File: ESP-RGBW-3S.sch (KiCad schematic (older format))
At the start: 41 parts, among them J1 12V IN, J2 PROG, J3 LED Str., J4 Temp. S., J5 Light. S., J6 PIR, Q1 IRLML0040TRPBF, Q2 IRLML0040TRPBF, Q3 IRLML0040TRPBF, Q4 IRLML0040TRPBF, SW1 Flash, U2 ESP-12E, U4 DCDC_LM2596

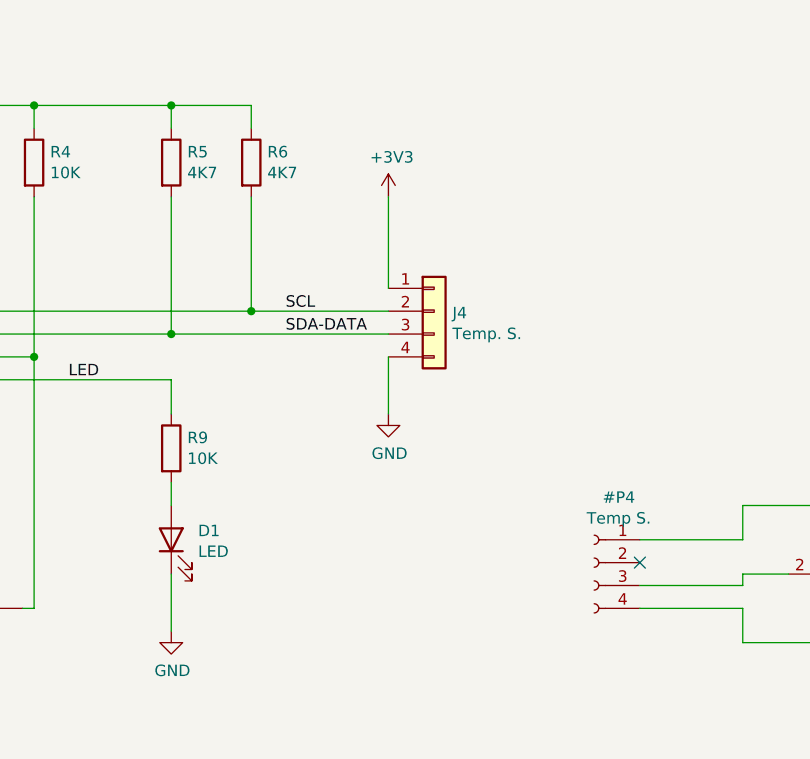
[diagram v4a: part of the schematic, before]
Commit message: oprional pull-down resistors for GPIO 4-5
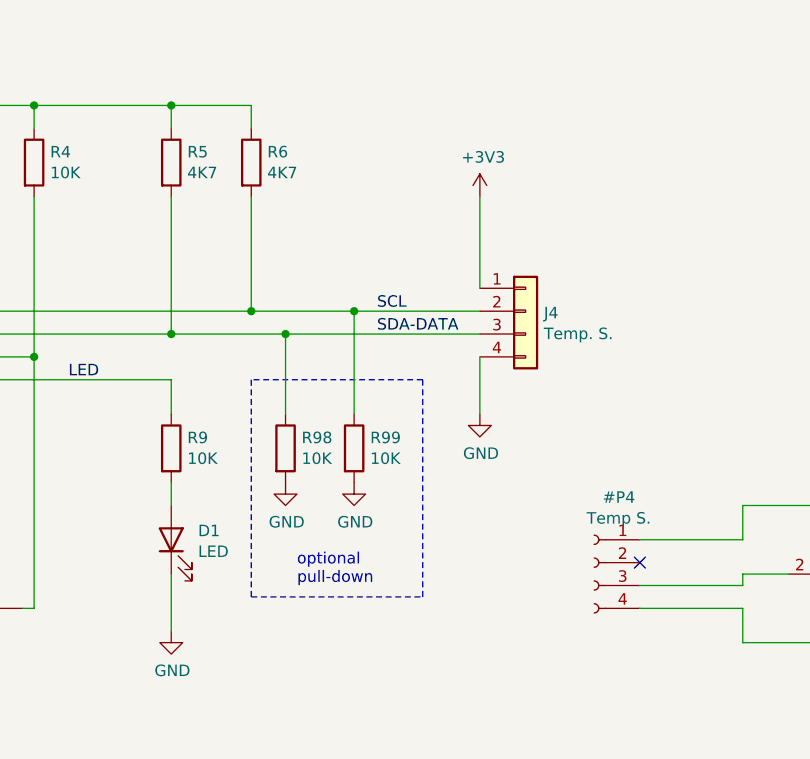
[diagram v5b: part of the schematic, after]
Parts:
- added R98, R99: 10K, Resistor_SMD:R_0805_2012Metric, symbol Device:R
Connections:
- net GND: now also R98.2, R99.2
- net SCL: now also R99.1
- net SDA-DATA: now also R98.1
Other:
- moved on the sheet: J4
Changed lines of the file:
@@
 L power:GND #PWR03
 U 1 1 609124D8
-P 6550 2200
-F 0 "#PWR03" H 6550 1950 50  0001 C CNN
-F 1 "GND" H 6555 2027 50  0000 C CNN
-F 2 "" H 6550 2200 50  0001 C CNN
-F 3 "" H 6550 2200 50  0001 C CNN
-	1    6550 2200
-	1    0    0    -1
-$EndComp
-Wire Wire Line
-	6550 1950 6550 2200
+P 6950 2200
+F 0 "#PWR03" H 6950 1950 50  0001 C CNN
+F 1 "GND" H 6955 2027 50  0000 C CNN
+F 2 "" H 6950 2200 50  0001 C CNN
+F 3 "" H 6950 2200 50  0001 C CNN
+	1    6950 2200
+	1    0    0    -1
+$EndComp
+Wire Wire Line
+	6950 1950 6950 2200
 Wire Wire Line
 	4100 1750 5950 1750
 Wire Wire Line
-	6550 1250 6550 1650
+	6950 1250 6950 1650
 $Comp
 L Device:R R6
@@
 Wire Wire Line
 	5950 1250 5950 1750
-Connection ~ 5950 1750
-Wire Wire Line
-	5950 1750 6550 1750
+Wire Wire Line
+	5950 1750 6400 1750
 Wire Wire Line
 	5600 1250 5600 1850
 Wire Wire Line
 	4100 1850 5600 1850
-Connection ~ 5600 1850
-Wire Wire Line
-	5600 1850 6550 1850
+Wire Wire Line
+	5600 1850 6100 1850
 $Comp
 L Connector_Generic:Conn_01x04 J4
 U 1 1 6090F6BA
-P 6750 1750
-F 0 "J4" H 6830 1742 50  0000 L CNN
-F 1 "Temp. S." H 6830 1651 50  0000 L CNN
-F 2 "Connector_Molex:Molex_KK-254_AE-6410-04A_1x04_P2.54mm_Vertical" H 6750 1750 50  0001 C CNN
-F 3 "~" H 6750 1750 50  0001 C CNN
-	1    6750 1750
-	1    0    0    -1
-$EndComp
-Text Label 6100 1850 0    50   ~ 0
+P 7150 1750
+F 0 "J4" H 7230 1742 50  0000 L CNN
+F 1 "Temp. S." H 7230 1651 50  0000 L CNN
+F 2 "Connector_Molex:Molex_KK-254_AE-6410-04A_1x04_P2.54mm_Vertical" H 7150 1750 50  0001 C CNN
+F 3 "~" H 7150 1750 50  0001 C CNN
+	1    7150 1750
+	1    0    0    -1
+$EndComp
+Text Label 6500 1850 0    50   ~ 0
 SDA-DATA
-Text Label 6100 1750 0    50   ~ 0
+Text Label 6500 1750 0    50   ~ 0
 SCL
 Wire Wire Line
@@
 L power:+3V3 #PWR02
 U 1 1 609155BA
-P 6550 1250
-F 0 "#PWR02" H 6550 1100 50  0001 C CNN
-F 1 "+3V3" H 6565 1423 50  0000 C CNN
-F 2 "" H 6550 1250 50  0001 C CNN
-F 3 "" H 6550 1250 50  0001 C CNN
-	1    6550 1250
+P 6950 1250
+F 0 "#PWR02" H 6950 1100 50  0001 C CNN
+F 1 "+3V3" H 6965 1423 50  0000 C CNN
+F 2 "" H 6950 1250 50  0001 C CNN
+F 3 "" H 6950 1250 50  0001 C CNN
+	1    6950 1250
 	1    0    0    -1
 $EndComp
@@
 	9550 600  9150 600
 $Comp
-L power:+3V3 #PWR?
+L power:+3V3 #PWR0108
 U 1 1 60B5BA99
 P 9150 600
-F 0 "#PWR?" H 9150 450 50  0001 C CNN
+F 0 "#PWR0108" H 9150 450 50  0001 C CNN
 F 1 "+3V3" H 9165 773 50  0000 C CNN
 F 2 "" H 9150 600 50  0001 C CNN
@@
 	9900 1750 9900 1500
 $Comp
-L power:GND #PWR?
+L power:GND #PWR0109
 U 1 1 60B6FB81
 P 9900 2150
-F 0 "#PWR?" H 9900 1900 50  0001 C CNN
+F 0 "#PWR0109" H 9900 1900 50  0001 C CNN
 F 1 "GND" H 9905 1977 50  0000 C CNN
 F 2 "" H 9900 2150 50  0001 C CNN
@@
 Text Notes 9000 1950 0    50   ~ 0
 optional\npull-down
+Connection ~ 5600 1850
+Connection ~ 5950 1750
+$Comp
+L Device:R R98
+U 1 1 60ADF053
+P 6100 2350
+F 0 "R98" H 6170 2396 50  0000 L CNN
+F 1 "10K" H 6170 2305 50  0000 L CNN
+F 2 "Resistor_SMD:R_0805_2012Metric" V 6030 2350 50  0001 C CNN
+F 3 "~" H 6100 2350 50  0001 C CNN
+	1    6100 2350
+	1    0    0    -1
+$EndComp
+$Comp
+L Device:R R99
+U 1 1 60ADFAE9
+P 6400 2350
+F 0 "R99" H 6470 2396 50  0000 L CNN
+F 1 "10K" H 6470 2305 50  0000 L CNN
+F 2 "Resistor_SMD:R_0805_2012Metric" V 6330 2350 50  0001 C CNN
+F 3 "~" H 6400 2350 50  0001 C CNN
+	1    6400 2350
+	1    0    0    -1
+$EndComp
+Wire Wire Line
+	6100 1850 6100 2200
+Connection ~ 6100 1850
+Wire Wire Line
+	6100 1850 6950 1850
+Wire Wire Line
+	6400 1750 6400 2200
+Connection ~ 6400 1750
+Wire Wire Line
+	6400 1750 6950 1750
+$Comp
+L power:GND #PWR0110
+U 1 1 60AEF13E
+P 6100 2500
+F 0 "#PWR0110" H 6100 2250 50  0001 C CNN
+F 1 "GND" H 6105 2327 50  0000 C CNN
+F 2 "" H 6100 2500 50  0001 C CNN
+F 3 "" H 6100 2500 50  0001 C CNN
+	1    6100 2500
+	1    0    0    -1
+$EndComp
+$Comp
+L power:GND #PWR0111
+U 1 1 60AEF684
+P 6400 2500
+F 0 "#PWR0111" H 6400 2250 50  0001 C CNN
+F 1 "GND" H 6405 2327 50  0000 C CNN
+F 2 "" H 6400 2500 50  0001 C CNN
+F 3 "" H 6400 2500 50  0001 C CNN
+	1    6400 2500
+	1    0    0    -1
+$EndComp
+Wire Notes Line
+	5950 2050 5950 3000
+Wire Notes Line
+	5950 3000 6700 3000
+Wire Notes Line
+	6700 3000 6700 2050
+Wire Notes Line
+	6700 2050 5950 2050
+Text Notes 6150 2950 0    50   ~ 0
+optional\npull-down
 $EndSCHEMATC

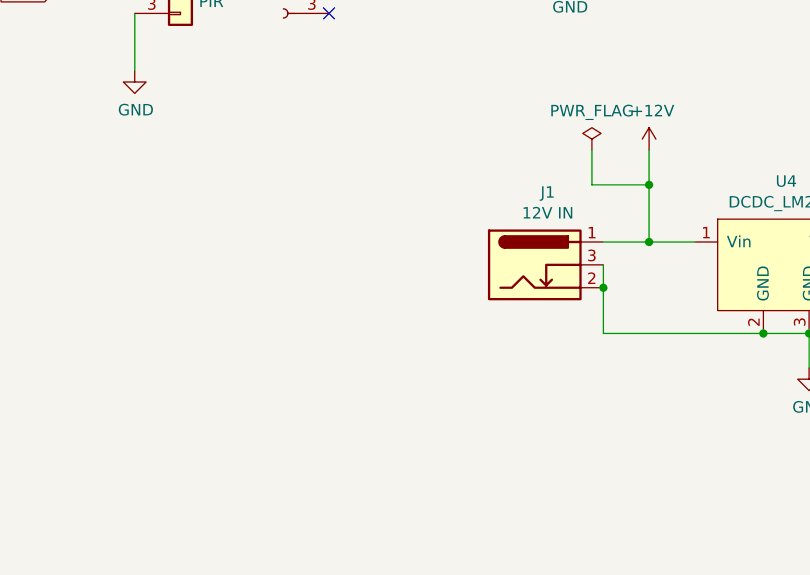
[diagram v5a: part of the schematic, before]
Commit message: oprional input power terminal
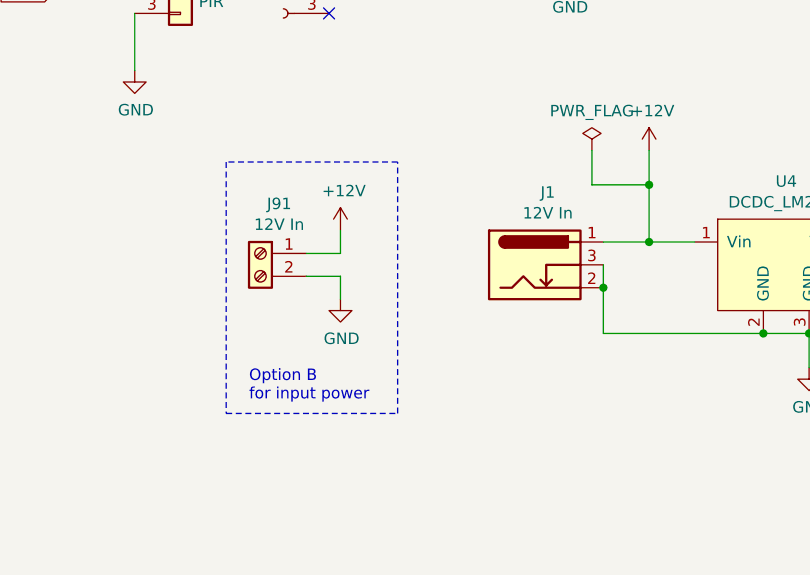
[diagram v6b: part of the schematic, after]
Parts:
- added J91: 12V In, symbol Connector:Screw_Terminal_01x02
- J1: value 12V IN -> 12V In
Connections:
- net +12V: now also J91.1 (Pin_1)
- net GND: now also J91.2 (Pin_2)
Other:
- note added: "Option B\nfor input power"
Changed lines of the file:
@@
 P 8550 5800
 F 0 "J1" H 8607 6117 50  0000 C CNN
-F 1 "12V IN" H 8607 6026 50  0000 C CNN
+F 1 "12V In" H 8607 6026 50  0000 C CNN
 F 2 "Connector_BarrelJack:BarrelJack_Horizontal" H 8600 5760 50  0001 C CNN
 F 3 "~" H 8600 5760 50  0001 C CNN
@@
 L power:+12V #PWR014
 U 1 1 60962EEC
-P 9050 5300
-F 0 "#PWR014" H 9050 5150 50  0001 C CNN
-F 1 "+12V" H 9065 5473 50  0000 C CNN
-F 2 "" H 9050 5300 50  0001 C CNN
-F 3 "" H 9050 5300 50  0001 C CNN
-	1    9050 5300
+P 7700 5650
+F 0 "#PWR014" H 7700 5500 50  0001 C CNN
+F 1 "+12V" H 7715 5823 50  0000 C CNN
+F 2 "" H 7700 5650 50  0001 C CNN
+F 3 "" H 7700 5650 50  0001 C CNN
+	1    7700 5650
 	1    0    0    -1
 $EndComp
@@
 Text Notes 6150 2950 0    50   ~ 0
 optional\npull-down
+$Comp
+L Connector:Screw_Terminal_01x02 J91
+U 1 1 60B29600
+P 7350 5750
+F 0 "J91" H 7268 5967 50  0000 C CNN
+F 1 "12V In" H 7268 5876 50  0000 C CNN
+F 2 "" H 7350 5750 50  0001 C CNN
+F 3 "~" H 7350 5750 50  0001 C CNN
+	1    7350 5750
+	-1   0    0    -1
+$EndComp
+$Comp
+L power:GND #PWR0112
+U 1 1 60B3AF54
+P 7700 5950
+F 0 "#PWR0112" H 7700 5700 50  0001 C CNN
+F 1 "GND" H 7705 5777 50  0000 C CNN
+F 2 "" H 7700 5950 50  0001 C CNN
+F 3 "" H 7700 5950 50  0001 C CNN
+	1    7700 5950
+	1    0    0    -1
+$EndComp
+$Comp
+L power:+12V #PWR0113
+U 1 1 60B3BF7D
+P 9050 5300
+F 0 "#PWR0113" H 9050 5150 50  0001 C CNN
+F 1 "+12V" H 9065 5473 50  0000 C CNN
+F 2 "" H 9050 5300 50  0001 C CNN
+F 3 "" H 9050 5300 50  0001 C CNN
+	1    9050 5300
+	1    0    0    -1
+$EndComp
+Wire Wire Line
+	7550 5750 7700 5750
+Wire Wire Line
+	7700 5750 7700 5650
+Wire Wire Line
+	7550 5850 7700 5850
+Wire Wire Line
+	7700 5850 7700 5950
+Wire Notes Line
+	7200 5350 7200 6450
+Wire Notes Line
+	7200 6450 7950 6450
+Wire Notes Line
+	7950 6450 7950 5350
+Wire Notes Line
+	7950 5350 7200 5350
+Text Notes 7300 6400 0    50   ~ 0
+Option B\nfor input power
 $EndSCHEMATC

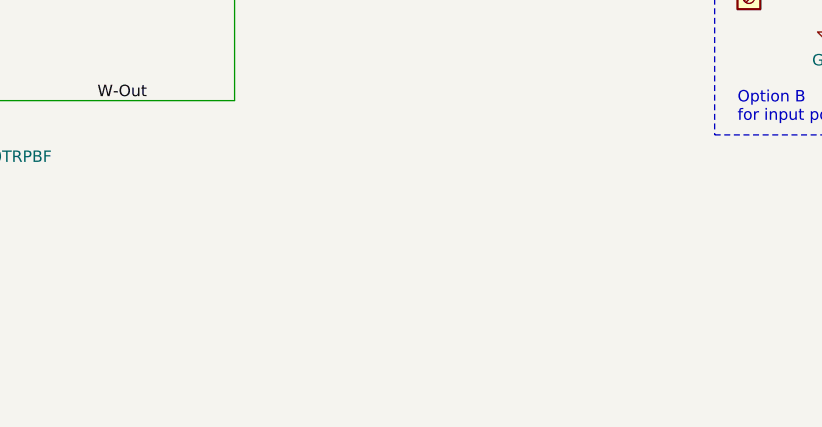
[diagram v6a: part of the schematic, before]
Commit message: alternative DC-DC convertor (MP1584)
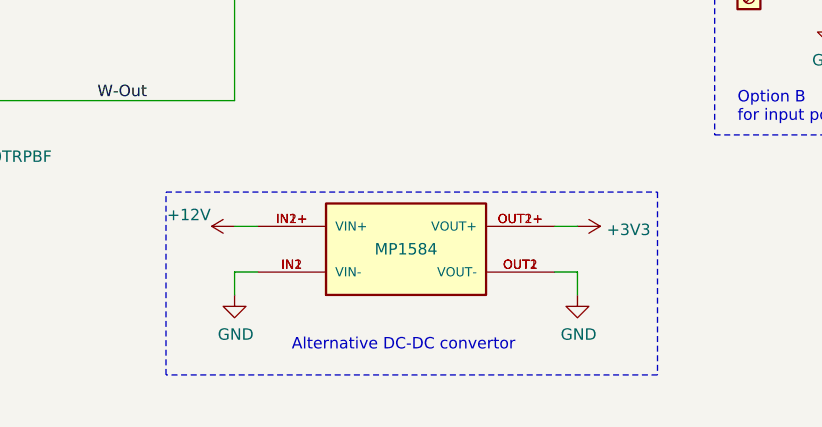
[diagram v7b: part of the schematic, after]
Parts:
- added U94: MP1584, MP1584:DC-BRICK, symbol MP1584:MP1584
- J91: footprint (none) -> TerminalBlock_Phoenix:TerminalBlock_Phoenix_MKDS-1,5-2_1x02_P5.00mm_Horizontal
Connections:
- net +12V: now also U94.IN1+ (VIN+), U94.IN2+ (VIN+)
- net +3V3: now also U94.OUT1+ (VOUT+), U94.OUT2+ (VOUT+)
- net GND: now also U94.IN1 (VIN-), U94.IN2 (VIN-), U94.OUT1 (VOUT-), U94.OUT2 (VOUT-)
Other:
- note added: "Alternative DC-DC convertor"
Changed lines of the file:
@@
 F 0 "J91" H 7268 5967 50  0000 C CNN
 F 1 "12V In" H 7268 5876 50  0000 C CNN
-F 2 "" H 7350 5750 50  0001 C CNN
+F 2 "TerminalBlock_Phoenix:TerminalBlock_Phoenix_MKDS-1,5-2_1x02_P5.00mm_Horizontal" H 7350 5750 50  0001 C CNN
 F 3 "~" H 7350 5750 50  0001 C CNN
 	1    7350 5750
@@
 Text Notes 7300 6400 0    50   ~ 0
 Option B\nfor input power
+$Comp
+L MP1584:MP1584 U94
+U 1 1 60B2F407
+P 5800 6950
+F 0 "U94" H 5800 6950 50  0001 L BNN
+F 1 "MP1584" H 5850 6950 50  0000 C CNN
+F 2 "MP1584:DC-BRICK" H 5800 6950 50  0001 L BNN
+F 3 "" H 5800 6950 50  0001 L BNN
+	1    5800 6950
+	1    0    0    -1
+$EndComp
+$Comp
+L power:GND #PWR0114
+U 1 1 60B307DC
+P 6600 7150
+F 0 "#PWR0114" H 6600 6900 50  0001 C CNN
+F 1 "GND" H 6605 6977 50  0000 C CNN
+F 2 "" H 6600 7150 50  0001 C CNN
+F 3 "" H 6600 7150 50  0001 C CNN
+	1    6600 7150
+	1    0    0    -1
+$EndComp
+$Comp
+L power:+3V3 #PWR0115
+U 1 1 60B4A7A1
+P 6600 6850
+F 0 "#PWR0115" H 6600 6700 50  0001 C CNN
+F 1 "+3V3" V 6615 6978 50  0000 L CNN
+F 2 "" H 6600 6850 50  0001 C CNN
+F 3 "" H 6600 6850 50  0001 C CNN
+	1    6600 6850
+	0    1    1    0
+$EndComp
+$Comp
+L power:+12V #PWR0116
+U 1 1 60B535FA
+P 5100 6850
+F 0 "#PWR0116" H 5100 6700 50  0001 C CNN
+F 1 "+12V" V 5150 7050 50  0000 C CNN
+F 2 "" H 5100 6850 50  0001 C CNN
+F 3 "" H 5100 6850 50  0001 C CNN
+	1    5100 6850
+	0    -1   -1   0
+$EndComp
+$Comp
+L power:GND #PWR0117
+U 1 1 60B53EF4
+P 5100 7150
+F 0 "#PWR0117" H 5100 6900 50  0001 C CNN
+F 1 "GND" H 5105 6977 50  0000 C CNN
+F 2 "" H 5100 7150 50  0001 C CNN
+F 3 "" H 5100 7150 50  0001 C CNN
+	1    5100 7150
+	1    0    0    -1
+$EndComp
+Wire Wire Line
+	5200 7050 5100 7050
+Wire Wire Line
+	5100 7050 5100 7150
+Wire Wire Line
+	6500 7050 6600 7050
+Wire Wire Line
+	6600 7050 6600 7150
+Wire Wire Line
+	6600 6850 6500 6850
+Wire Wire Line
+	5100 6850 5200 6850
+Wire Notes Line
+	4800 6700 6950 6700
+Wire Notes Line
+	6950 6700 6950 7500
+Wire Notes Line
+	6950 7500 4800 7500
+Wire Notes Line
+	4800 7500 4800 6700
+Text Notes 5350 7400 0    50   ~ 0
+Alternative DC-DC convertor
 $EndSCHEMATC

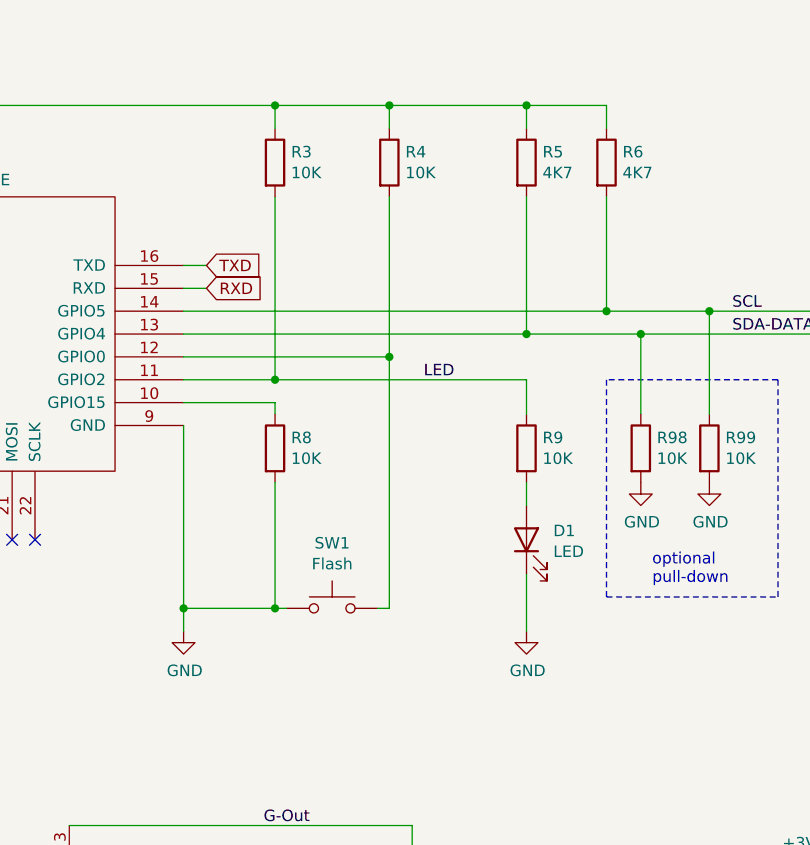
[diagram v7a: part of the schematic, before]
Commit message: status LED controlled by low-velef on mcu pin
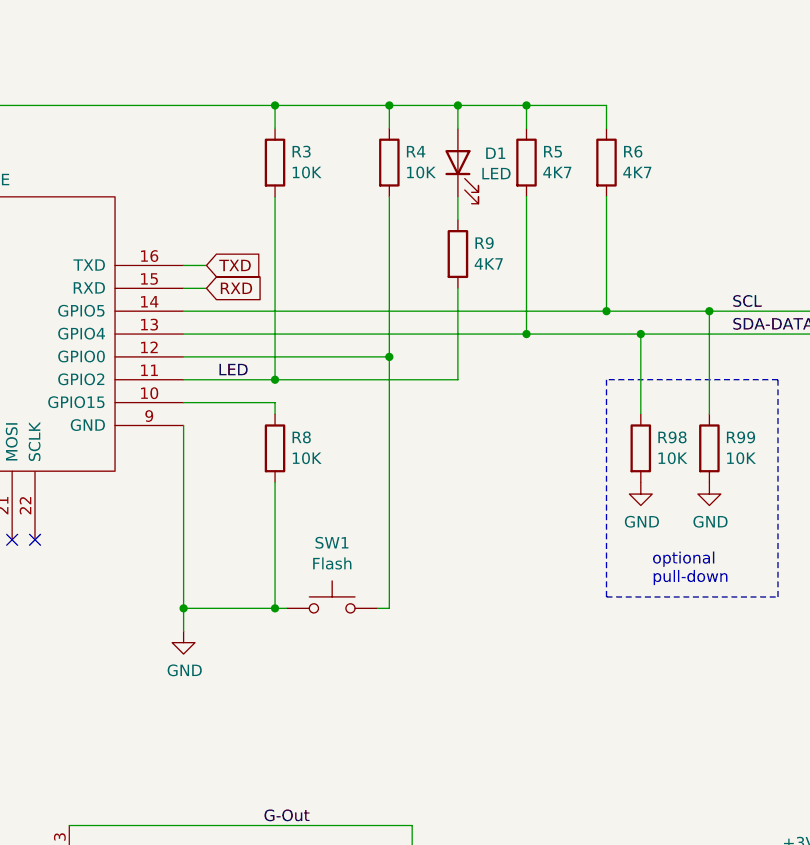
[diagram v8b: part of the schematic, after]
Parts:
- R9: value 10K -> 4K7
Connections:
- net +3V3: now also D1.2 (A)
- net GND: no longer D1.1 (K)
- net LED: now also R9.2; no longer R9.1
- new net: D1.1 (K), R9.1
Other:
- moved on the sheet: D1, R9
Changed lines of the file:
@@
 	5600 950  5600 850
 Wire Wire Line
-	5600 850  5000 850
+	5600 850  5300 850
 Wire Wire Line
 	5950 950  5950 850
@@
 L Device:LED D1
 U 1 1 60947566
-P 5600 2750
-F 0 "D1" V 5639 2633 50  0000 R CNN
-F 1 "LED" V 5548 2633 50  0000 R CNN
-F 2 "LED_THT:LED_D1.8mm_W3.3mm_H2.4mm" H 5600 2750 50  0001 C CNN
-F 3 "~" H 5600 2750 50  0001 C CNN
-	1    5600 2750
+P 5300 1100
+F 0 "D1" V 5339 983 50  0000 R CNN
+F 1 "LED" V 5250 1000 50  0000 R CNN
+F 2 "LED_THT:LED_D1.8mm_W3.3mm_H2.4mm" H 5300 1100 50  0001 C CNN
+F 3 "~" H 5300 1100 50  0001 C CNN
+	1    5300 1100
 	0    -1   -1   0
 $EndComp
-Wire Wire Line
-	4500 2050 5600 2050
-Connection ~ 4500 2050
 Wire Wire Line
 	4500 2150 4500 2200
@@
 L Device:R R9
 U 1 1 6094FB34
-P 5600 2350
-F 0 "R9" H 5670 2396 50  0000 L CNN
-F 1 "10K" H 5670 2305 50  0000 L CNN
-F 2 "Resistor_SMD:R_0805_2012Metric" V 5530 2350 50  0001 C CNN
-F 3 "~" H 5600 2350 50  0001 C CNN
-	1    5600 2350
-	1    0    0    -1
-$EndComp
-Wire Wire Line
-	5600 2050 5600 2200
+P 5300 1500
+F 0 "R9" H 5370 1546 50  0000 L CNN
+F 1 "4K7" H 5370 1455 50  0000 L CNN
+F 2 "Resistor_SMD:R_0805_2012Metric" V 5230 1500 50  0001 C CNN
+F 3 "~" H 5300 1500 50  0001 C CNN
+	1    5300 1500
+	1    0    0    -1
+$EndComp
 Wire Wire Line
 	4100 3050 4100 3150
-$Comp
-L power:GND #PWR08
-U 1 1 60954D3D
-P 5600 3150
-F 0 "#PWR08" H 5600 2900 50  0001 C CNN
-F 1 "GND" H 5605 2977 50  0000 C CNN
-F 2 "" H 5600 3150 50  0001 C CNN
-F 3 "" H 5600 3150 50  0001 C CNN
-	1    5600 3150
-	1    0    0    -1
-$EndComp
-Wire Wire Line
-	5600 2500 5600 2600
-Wire Wire Line
-	5600 2900 5600 3150
 $Comp
 L Device:R R7
@@
 Wire Wire Line
 	10400 6100 10050 6100
-Text Label 5150 2050 0    50   ~ 0
+Text Label 4250 2050 0    50   ~ 0
 LED
 Text Label 6500 4600 0    50   ~ 0
@@
 Text Notes 5350 7400 0    50   ~ 0
 Alternative DC-DC convertor
+Wire Wire Line
+	5300 950  5300 850
+Connection ~ 5300 850
+Wire Wire Line
+	5300 850  5000 850
+Wire Wire Line
+	5300 1350 5300 1250
+Wire Wire Line
+	5300 1650 5300 2050
+Wire Wire Line
+	5300 2050 4500 2050
+Connection ~ 4500 2050
 $EndSCHEMATC
